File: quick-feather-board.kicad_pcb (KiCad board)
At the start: 4 copper layers, 58.4 x 22.9 mm, 99 parts, among them IC1 EOS-S3-QFN, J1 61300211121, J2 1x12_pinhead, J3 1x16_pinhead, J4 S2B-PH-SM4-TB_LF__SN_, J5 0473460001, J6 FTSH-105-01-L-DV-K, J7 61300211121, J8 2x8_pinhead, M1 mounting_pad, M2 mounting_pad, M3 mounting_pad, M4 mounting_pad, Q1 NX3008CBKV, Q2 2N7002PV, Q3 2N7002PV, U1 TPS62821DLCR, U2 MCP73831T-2ACI_OT, U3 GD25Q16CWIGR, U4 DPS310, U5 MC3635, X1 ECS-_327-12_5-34B-TR

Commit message: Updated library references
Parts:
- C1, C14, C16, C2, C4, C5: footprint quicklogic-quick-feather-board-footprints:0603-cap -> quick-feather-board-footprints:0603-cap
- C10, C11, C12, C13, C15, C17, C18, C3, C6, C7, C8, C9: footprint quicklogic-quick-feather-board-footprints:0402-cap -> quick-feather-board-footprints:0402-cap
- D1: footprint quicklogic-quick-feather-board-footprints:SOD-123 -> quick-feather-board-footprints:SOD-123
- D11, D3, D5: footprint quicklogic-quick-feather-board-footprints:SOT-3 -> quick-feather-board-footprints:SOT-3
- D2: footprint quicklogic-quick-feather-board-footprints:LED_0603 -> quick-feather-board-footprints:LED_0603
- D4: footprint quicklogic-quick-feather-board-footprints:LED-PLCC4_3.2x2.8mm_B -> quick-feather-board-footprints:LED-PLCC4_3.2x2.8mm_B
- D6: footprint quicklogic-quick-feather-board-footprints:SOD-323-SD05 -> quick-feather-board-footprints:SOD-323-SD05
- IC1: footprint quicklogic-quick-feather-board-footprints:QFN-64_EP_8.5x8.5_EOS -> quick-feather-board-footprints:QFN-64_EP_8.5x8.5_EOS
- J1, J7: footprint quicklogic-quick-feather-board-footprints:PinHeader_1x2_P2.54_Drill0.9mm -> quick-feather-board-footprints:PinHeader_1x2_P2.54_Drill0.9mm
- J2: footprint quicklogic-quick-feather-board-footprints:1x12_pinhead -> quick-feather-board-footprints:1x12_pinhead
- J3: footprint quicklogic-quick-feather-board-footprints:1x16_pinhead -> quick-feather-board-footprints:1x16_pinhead
- J4: footprint quicklogic-quick-feather-board-footprints:PinHeader_2x1mm_P2mm_SMD_RA -> quick-feather-board-footprints:PinHeader_2x1mm_P2mm_SMD_RA
- J5: footprint quicklogic-quick-feather-board-footprints:USB_Micro_B_Female_0473460001 -> quick-feather-board-footprints:USB_Micro_B_Female_0473460001
- J6: footprint quicklogic-quick-feather-board-footprints:PinHeader_2x5_P1.27_SMD -> quick-feather-board-footprints:PinHeader_2x5_P1.27_SMD
- J8: footprint quicklogic-quick-feather-board-footprints:2x8_pinhead -> quick-feather-board-footprints:2x8_pinhead
- L1: footprint quicklogic-quick-feather-board-footprints:0806 -> quick-feather-board-footprints:0806
- M1, M2, M3, M4: footprint quicklogic-quick-feather-board-footprints:MPAD -> quick-feather-board-footprints:MPAD
- MIC1: footprint quicklogic-quick-feather-board-footprints:IM69D130 -> quick-feather-board-footprints:IM69D130
- N1: footprint quicklogic-quick-feather-board-footprints:oshw-logo -> quick-feather-board-footprints:oshw-logo
- N2: footprint quicklogic-quick-feather-board-footprints:LOGO -> quick-feather-board-footprints:LOGO
- Q1, Q2, Q3: footprint quicklogic-quick-feather-board-footprints:SOT-563 -> quick-feather-board-footprints:SOT-563
- R1, R10, R11, R12, R13, R14, R15, R16, R17, R18, R19, R2, R20, R21, R22, R23, R24, R25, R26, R28, R29, R3, R31, R32, R34, R35, R36, R37, R38, R39, R4, R40, R5, R6, R7, R8, R9: footprint quicklogic-quick-feather-board-footprints:0402-res -> quick-feather-board-footprints:0402-res
- R30, R33, R41, R42: footprint quicklogic-quick-feather-board-footprints:R_Array_Convex_8x0602 -> quick-feather-board-footprints:R_Array_Convex_8x0602
- S1, S2: footprint quicklogic-quick-feather-board-footprints:SW_SPST_4.2x2.8 -> quick-feather-board-footprints:SW_SPST_4.2x2.8
- TP1, TP2, TP6: footprint quicklogic-quick-feather-board-footprints:Testpoint_smd_1mm -> quick-feather-board-footprints:Testpoint_smd_1mm
- TP4, TP5: footprint quicklogic-quick-feather-board-footprints:Testpoint_THT_Drill0.9mm -> quick-feather-board-footprints:Testpoint_THT_Drill0.9mm
- U1: footprint quicklogic-quick-feather-board-footprints:QFN-8_2x1mm -> quick-feather-board-footprints:QFN-8_2x1mm
- U2: footprint quicklogic-quick-feather-board-footprints:SOT-753 -> quick-feather-board-footprints:SOT-753
- U3: footprint quicklogic-quick-feather-board-footprints:GD25Q16CWIG -> quick-feather-board-footprints:GD25Q16CWIG
- U4: footprint quicklogic-quick-feather-board-footprints:PG-VLGA-8-2 -> quick-feather-board-footprints:PG-VLGA-8-2
- U5: footprint quicklogic-quick-feather-board-footprints:MC3635 -> quick-feather-board-footprints:MC3635
- X1: footprint quicklogic-quick-feather-board-footprints:SMD-2_3.2x1.5mm -> quick-feather-board-footprints:SMD-2_3.2x1.5mm

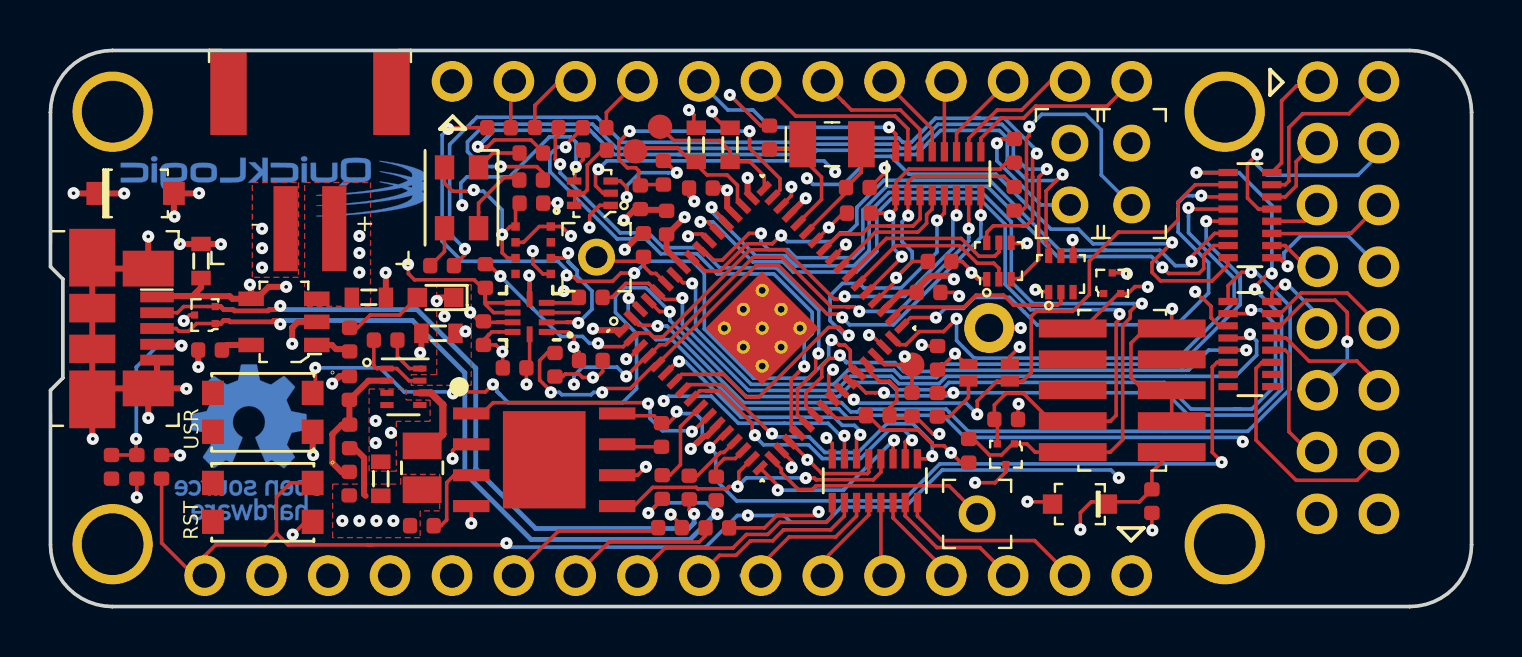
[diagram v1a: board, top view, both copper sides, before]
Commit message: Updated PCB layout for charger with delayed startup
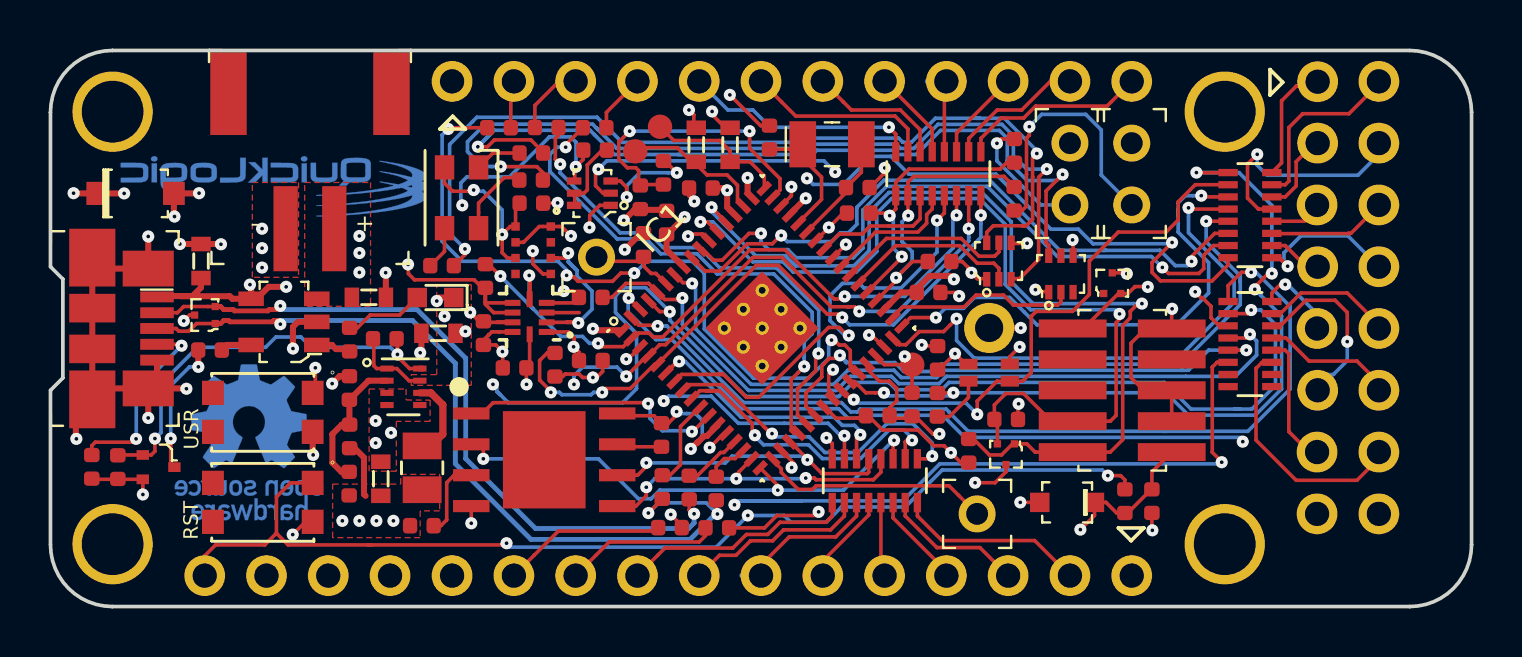
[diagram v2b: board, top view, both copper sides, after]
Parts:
- removed R35: R_22R_0402, quick-feather-board-footprints:0402-res
- added C19: C_1u_0402, quick-feather-board-footprints:0402-cap, F.Cu at (125.9, 110.7)
- added Q4: DMG1012T-7, quick-feather-board-footprints:SOT-523, F.Cu at (127.5, 110.7)
- IC1: footprint quick-feather-board-footprints:QFN-64_EP_8.5x8.5_EOS -> quick-feather-board-footprints:QFN-64_8.5x8.5_EOS
- R1: value R_100k_0402 -> R_1M5_0402; footprint quick-feather-board-footprints:0402-res -> antmicro-footprints:0402-res
- moved R6 39.6 mm to (167.3, 112.1), turned to 90 degrees
- moved R36 1.85 mm to (124.8, 110.7)
- moved D6 0.53 mm to (164.9, 112.2)
- moved R1 0.06 mm to (136.8, 105.4)
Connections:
- net /NC renamed Net-(U5-Pad3)
- net /S3IO_35_SPI_MST_CS3 renamed Net-(IC1-Pad18)
- net Net-(R1-Pad2) renamed /PG
- R2 pad 2: GND -> Net-(Q4-Pad3)
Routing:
- net /PG: track 1.90 -> 17.2 mm, vias 0 -> 2
- net /SPI_MST_CLK: track 18.4 -> 12.7 mm
- net Net-(Q4-Pad3): track 0.00 -> 5.56 mm, vias 0 -> 2
- net /SYS_RST: track 76.6 -> 71.9 mm
- net /SPI_MST_MISO: track 25.7 -> 22.1 mm
- net /S3IO_40: track 29.0 -> 31.9 mm, vias 2 -> 3
- net GND: track 89.5 -> 90.8 mm, vias 51 -> 50
- net /USR_BUTTON: track 56.9 -> 57.7 mm, vias 5 -> 4
- net +3V3: track 59.1 -> 58.6 mm, vias 22 -> 21
- net /SPI_MST_MOSI: vias 2 -> 3

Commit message: BOM and internal library updated
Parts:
- R1: footprint antmicro-footprints:0402-res -> quick-feather-board-footprints:0402-res
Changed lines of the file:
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@@
     (add_net +VBUS)
   )
-  (module antmicro-footprints:0402-res (layer Top)
+  (module quick-feather-board-footprints:0402-res (layer Top)
     (at 136.8453 105.4267)
     (descr "Resistor SMD 0402 (1005 Metric), square (rectangular) end terminal, IPC_7351 nominal, (Body size source: http://www.tortai-tech.com/upload/download/2011102023233369053.pdf), generated with kicad-footprint-generator")
@@
     (pad 1 smd roundrect (at -0.485 0) (size 0.59 0.64) (layers Top F.Paste F.Mask) (roundrect_rratio 0.25)
       (net 28 +VBUS))
-    (model ${ANT3DMDL}/0402-res.step
+    (model ${KIPRJMOD}/lib/3d-models/0402-res.step
       (offset (xyz 0 0 -0.01))
       (scale (xyz 1 1 1))
